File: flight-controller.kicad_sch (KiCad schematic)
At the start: 9 parts, among them J1 USB_C_Receptacle_USB2.0, U1 AT32F435RGT7, U2 BMI270, U3 BMP280, U4 W25N01GVZEIG, U5 AT7456E, U6 TPS54335A, U7 TPS54335A, U8 TLV75733PDBV

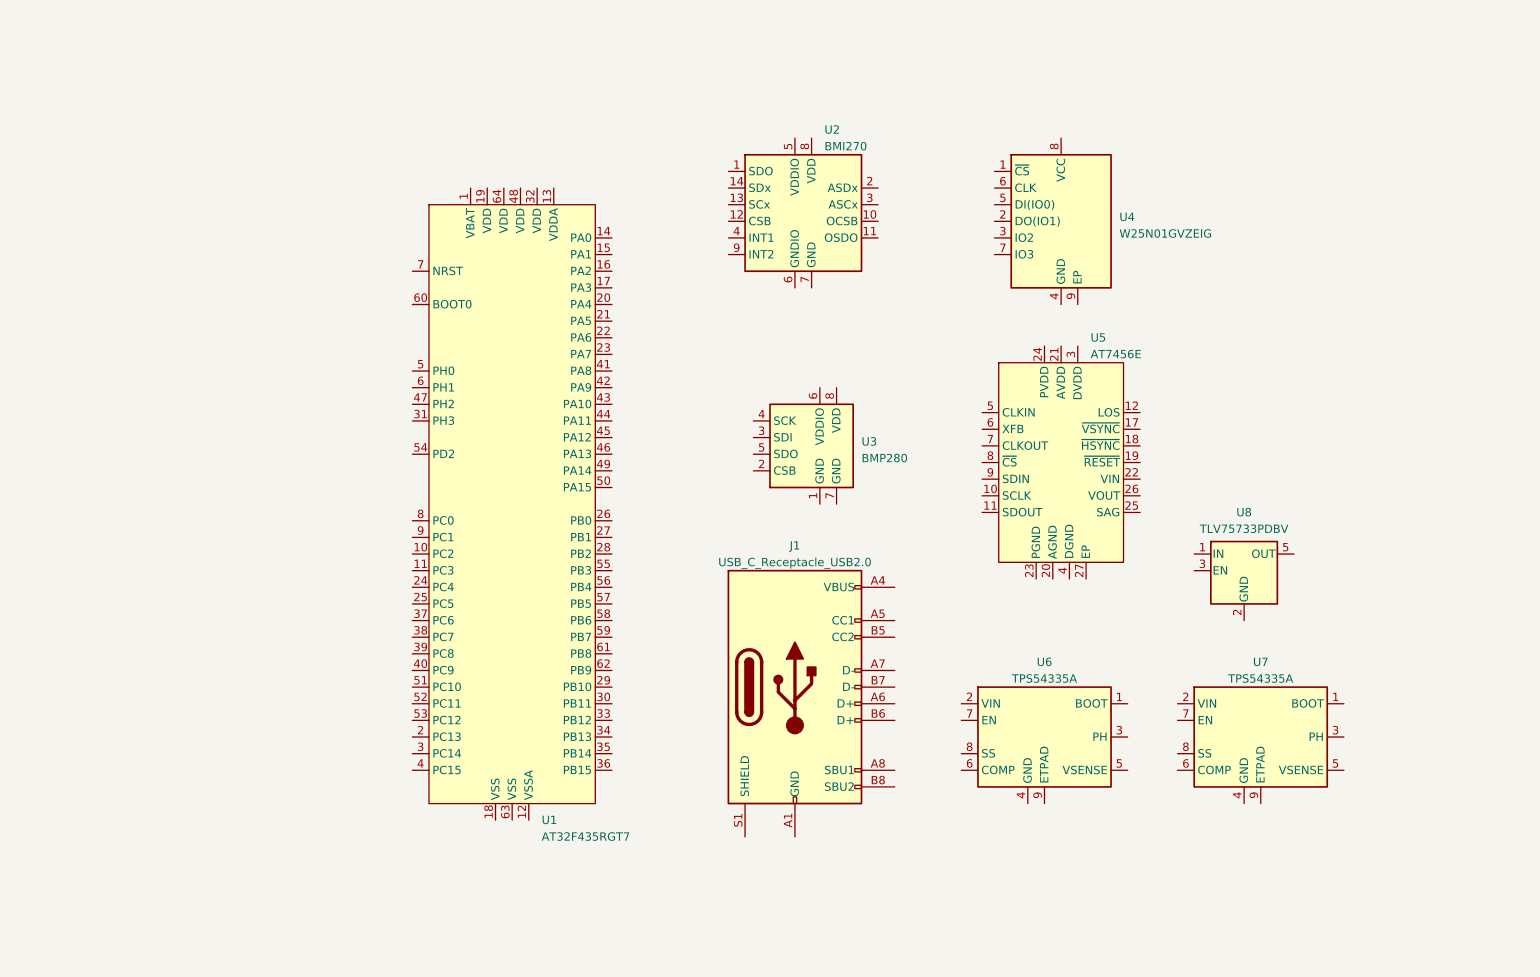
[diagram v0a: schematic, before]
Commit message: Begin AT32 pin planning, add USB footprint, schematic basics
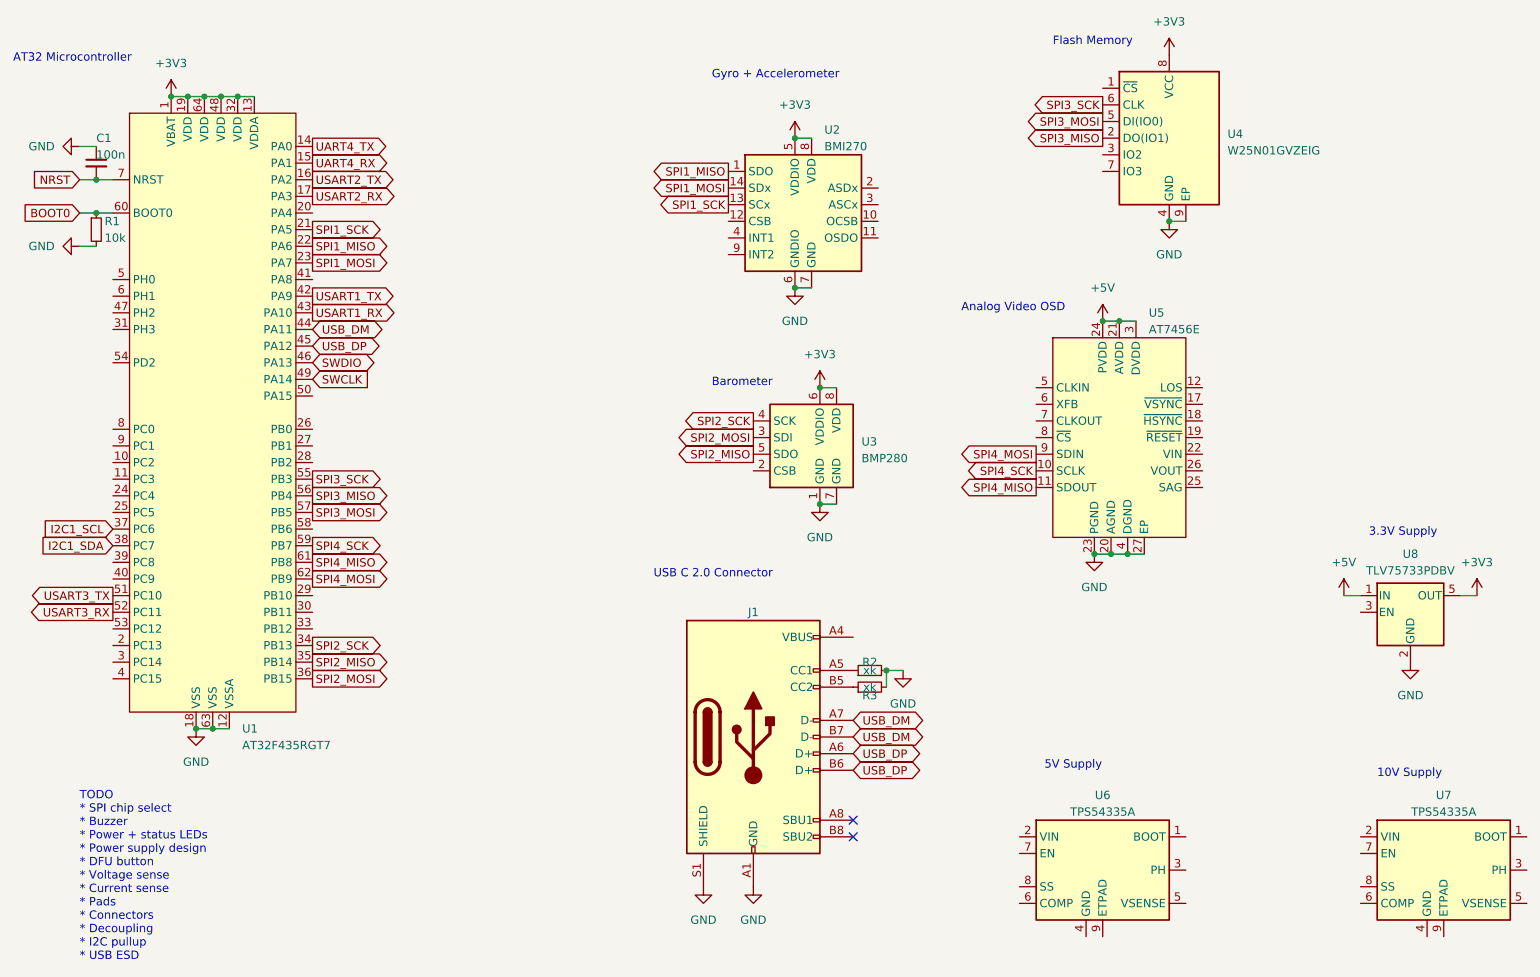
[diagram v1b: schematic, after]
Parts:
- added C1: 100n, symbol Device:C_Small
- added R1: 10k, symbol Device:R_Small
- added R2, R3: xk, symbol Device:R_Small
- J1: footprint (none) -> flight-controller:TYPE-C-31-M-12
- U1: footprint (none) -> Package_QFP:LQFP-64_10x10mm_P0.5mm
- U5: footprint (none) -> Package_SO:TSSOP-28-1EP_4.4x9.7mm_P0.65mm
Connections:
- net +5V: now reaches U8.1 (IN)
- net +5V: now also U5.21 (AVDD), U5.24 (PVDD), U5.3 (DVDD)
- net GND: now reaches U8.2 (GND)
- net GND: now also J1.A1 (GND), J1.A12 (GND), J1.B1 (GND), J1.B12 (GND), J1.S1 (SHIELD), U1.12 (VSSA), U1.18 (VSS), U1.63 (VSS), U2.6 (GNDIO), U2.7 (GND), U3.1 (GND), U3.7 (GND), U4.4 (GND), U4.9 (EP), U5.20 (AGND), U5.23 (PGND), U5.27 (EP), U5.4 (DGND), C1.1, R1.2, R2.2, R3.2
- net +3V3: now reaches U8.5 (OUT)
- net +3V3: now also U1.1 (VBAT), U1.13 (VDDA), U1.19 (VDD), U1.32 (VDD), U1.48 (VDD), U1.64 (VDD), U2.5 (VDDIO), U2.8 (VDD), U3.6 (VDDIO), U3.8 (VDD), U4.8 (VCC)
- net SPI2_MOSI: now reaches U3.3 (SDI)
- net SPI2_MOSI: now also U1.36 (PB15)
- net SPI2_SCK: now reaches U3.4 (SCK)
- net SPI2_SCK: now also U1.34 (PB13)
- net SPI2_MISO: now reaches U3.5 (SDO)
- net SPI2_MISO: now also U1.35 (PB14)
- net SPI1_MISO: now reaches U2.1 (SDO)
- net SPI1_MISO: now also U1.22 (PA6)
- net SPI1_SCK: now reaches U2.13 (SCx)
- net SPI1_SCK: now also U1.21 (PA5)
- net SPI1_MOSI: now reaches U2.14 (SDx)
- net SPI1_MOSI: now also U1.23 (PA7)
- net UART4_TX: now reaches U1.14 (PA0)
- net UART4_RX: now reaches U1.15 (PA1)
- net USART2_TX: now reaches U1.16 (PA2)
- net USART2_RX: now reaches U1.17 (PA3)
- net I2C1_SCL: now reaches U1.37 (PC6)
- net I2C1_SDA: now reaches U1.38 (PC7)
- net USART1_TX: now reaches U1.42 (PA9)
- net USART1_RX: now reaches U1.43 (PA10)
- net USB_DM: now reaches U1.44 (PA11)
- net USB_DM: now also J1.A7 (D-), J1.B7 (D-)
- net USB_DP: now reaches U1.45 (PA12)
- net USB_DP: now also J1.A6 (D+), J1.B6 (D+)
- net SWDIO: now reaches U1.46 (PA13)
- net SWCLK: now reaches U1.49 (PA14)
- net USART3_TX: now reaches U1.51 (PC10)
- net USART3_RX: now reaches U1.52 (PC11)
- net SPI3_SCK: now reaches U1.55 (PB3)
- net SPI3_SCK: now also U4.6 (CLK)
- net SPI3_MISO: now reaches U1.56 (PB4)
- net SPI3_MISO: now also U4.2 (DO(IO1))
- net SPI3_MOSI: now reaches U1.57 (PB5)
- net SPI3_MOSI: now also U4.5 (DI(IO0))
- net SPI4_SCK: now reaches U1.59 (PB7)
- net SPI4_SCK: now also U5.10 (SCLK)
- net BOOT0: now reaches U1.60 (BOOT0)
- net BOOT0: now also R1.1
- net SPI4_MISO: now reaches U1.61 (PB8)
- net SPI4_MISO: now also U5.11 (SDOUT)
- net SPI4_MOSI: now reaches U1.62 (PB9)
- net SPI4_MOSI: now also U5.9 (SDIN)
- net NRST: now reaches U1.7 (NRST)
- net NRST: now also C1.2
- net at J1.A5 (CC1): now also R2.1
- net at J1.B5 (CC2): now also R3.1
- no-connect marks 0 -> 2
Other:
- note added: "10V Supply"
- note added: "3.3V Supply"
- note added: "5V Supply"
- note added: "AT32 Microcontroller"
- note added: "Analog Video OSD"
- note added: "Barometer"
- note added: "Flash Memory"
- note added: "Gyro + Accelerometer"
- note added: "TODO * SPI chip select * Buzzer * Power + status LEDs * Power supply design * DFU button * Voltage sense * Current sense * Pads * Connectors * Decoupling * I2C pullup * USB ESD"
- note added: "USB C 2.0 Connector"
- moved on the sheet: J1, U1, U4, U5, U6, U7, U8

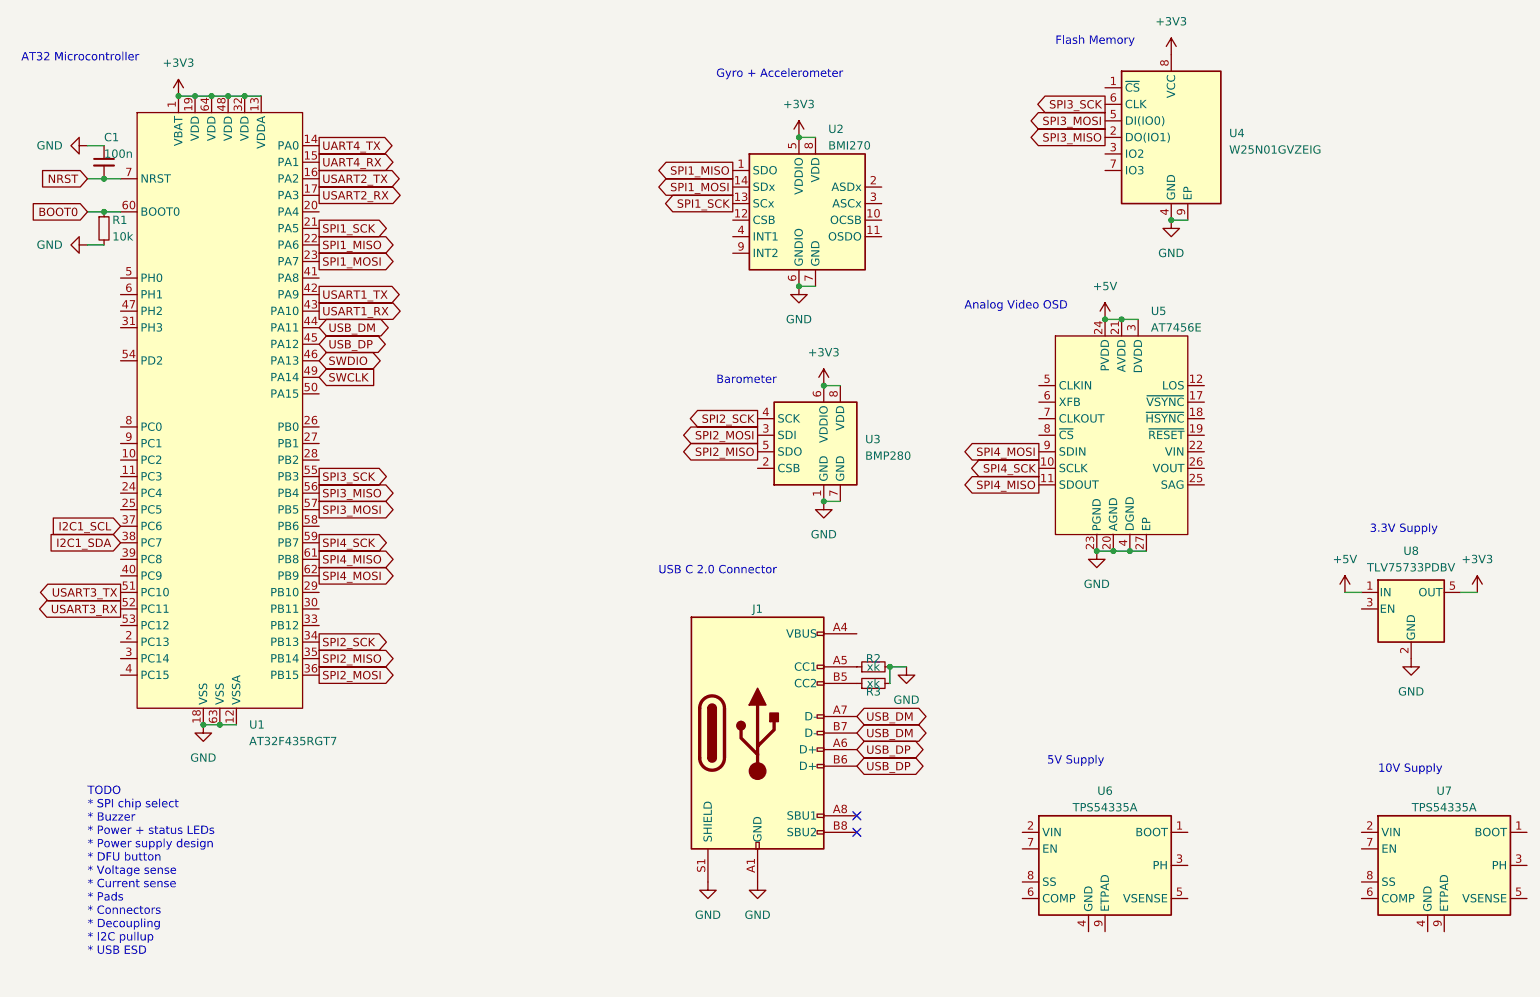
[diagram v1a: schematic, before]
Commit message: Finish majority of MCU pin mapping
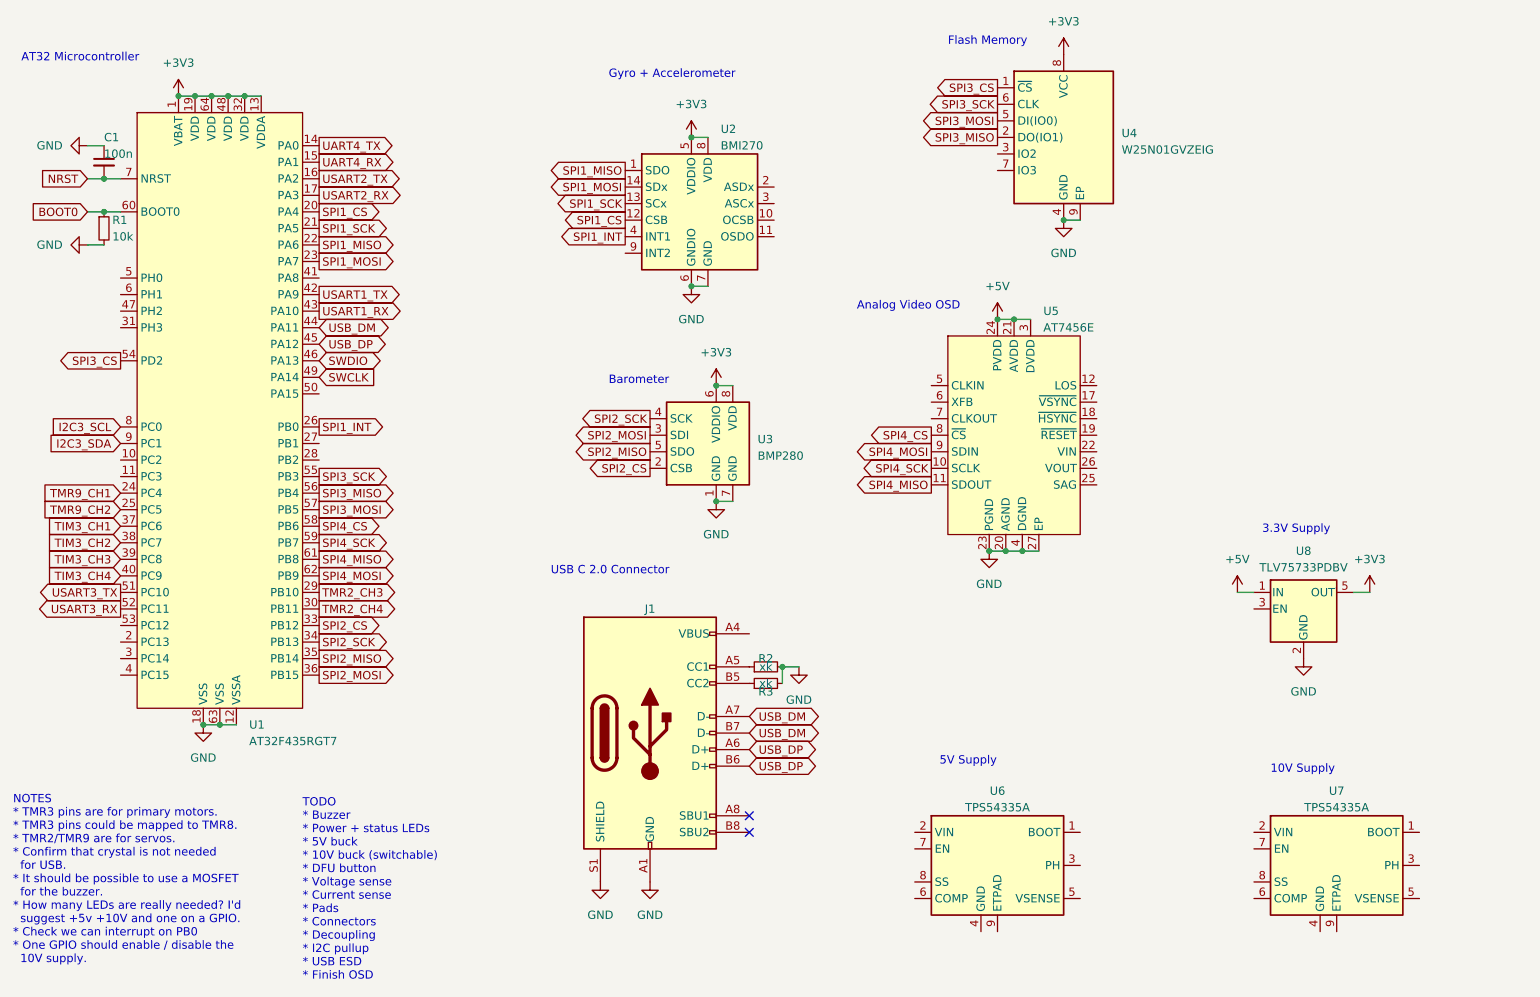
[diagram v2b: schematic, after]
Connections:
- net SPI2_CS: now reaches U3.2 (CSB)
- net SPI2_CS: now also U1.33 (PB12)
- net SPI1_CS: now reaches U2.12 (CSB)
- net SPI1_CS: now also U1.20 (PA4)
- net SPI1_INT: now reaches U2.4 (INT1)
- net SPI1_INT: now also U1.26 (PB0)
- net TMR9_CH1: now reaches U1.24 (PC4)
- net TMR9_CH2: now reaches U1.25 (PC5)
- net TMR2_CH3: now reaches U1.29 (PB10)
- net TMR2_CH4: now reaches U1.30 (PB11)
- net TIM3_CH3: now reaches U1.39 (PC8)
- net TIM3_CH4: now reaches U1.40 (PC9)
- net SPI3_CS: now reaches U1.54 (PD2)
- net SPI3_CS: now also U4.1 (~{CS})
- net SPI4_CS: now reaches U1.58 (PB6)
- net SPI4_CS: now also U5.8 (~{CS})
- net I2C3_SCL: now reaches U1.8 (PC0)
- net I2C3_SDA: now reaches U1.9 (PC1)
- net I2C1_SCL renamed TIM3_CH1
- net I2C1_SDA renamed TIM3_CH2
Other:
- note added: "NOTES * TMR3 pins are for primary motors. * TMR3 pins could be mapped to TMR8. * TMR2/TMR9 are for servos. * Confirm that crystal is not needed for USB. * It should be possible to use a MOSFET for the buzzer. * How many LEDs are really needed? I'd suggest +5v +10V and one on a GPIO. * Check we can interrupt on PB0 * One GPIO should enable / disable the 10V supply."
- note added: "TODO * Buzzer * Power + status LEDs * 5V buck * 10V buck (switchable) * DFU button * Voltage sense * Current sense * Pads * Connectors * Decoupling * I2C pullup * USB ESD * Finish OSD"
- note removed: "TODO * SPI chip select * Buzzer * Power + status LEDs * Power supply design * DFU button * Voltage sense * Current sense * Pads * Connectors * Decoupling * I2C pullup * USB ESD"
- moved on the sheet: J1, R2, R3, U2, U3, U4, U5, U6, U7, U8

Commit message: Tidy up schematic, fix label directions, add decupling caps, pullups, buttons, LEDs
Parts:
- added C10, C11, C12, C13, C14, C15, C2, C3, C4, C5, C6, C7, C8, C9: 100n, symbol Device:C_Small
- added D1: BLUE, symbol Device:LED
- added D2: GREEN, symbol Device:LED
- added D3: RED, symbol Device:LED
- added D4: YELLOW, symbol Device:LED
- added R4, R5: 10k, symbol Device:R_Small
- added R6: 220, symbol Device:R_Small
- added R7, R8, R9: ???, symbol Device:R_Small
- added SW1: SW_Push, symbol Switch:SW_Push
- R2, R3: value xk -> 5.1k
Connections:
- net +3V3: now also U2.2 (ASDx), U2.3 (ASCx), R4.2, R5.2, SW1.2
- net BOOT0: now also SW1.1
- net GND: now also D3.1 (K), D4.1 (K)
- net I2C3_SCL: now also R4.1
- net I2C3_SDA: now also R5.1
- net +BATT: now reaches U7.2 (VIN)
- net +BATT: now also U6.2 (VIN)
- new net: D2.2 (A), R7.2
- new net: D3.2 (A), R8.2
- new net: R6.1, R7.1, R8.1
- new net: D1.2 (A), R6.2
- new net: D4.2 (A), R9.2
- new net +10V: R9.1
- new net LED1: D1.1 (K)
- new net LED2: D2.1 (K)
- no-connect marks 2 -> 7
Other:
- note added: "3v3 or 5V"
- note added: "Buttons and LEDs"
- note added: "Buzzer"
- note added: "Connectors"
- note added: "I2C Pullup"
- note added: "NOTES * TMR3 pins are for primary motors. * TMR3 pins could be mapped to TMR8. * TMR2/TMR9 are for servos. * Confirm that crystal is not needed for USB. * It should be possible to use a MOSFET for the buzzer. * How many LEDs are really needed? I'd suggest +5v +10V and one on a GPIO. * Check we can interrupt on PB0 * One GPIO should enable / disable the 10V supply. * LED supplies can be 5V as long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"
- note added: "TODO * Buzzer * 5V buck * 10V buck (switchable) * Voltage sense * Current sense * Pads * Connectors * USB ESD * Finish OSD"
- note added: "USB ESD"
- note removed: "NOTES * TMR3 pins are for primary motors. * TMR3 pins could be mapped to TMR8. * TMR2/TMR9 are for servos. * Confirm that crystal is not needed for USB. * It should be possible to use a MOSFET for the buzzer. * How many LEDs are really needed? I'd suggest +5v +10V and one on a GPIO. * Check we can interrupt on PB0 * One GPIO should enable / disable the 10V supply."
- note removed: "TODO * Buzzer * Power + status LEDs * 5V buck * 10V buck (switchable) * DFU button * Voltage sense * Current sense * Pads * Connectors * Decoupling * I2C pullup * USB ESD * Finish OSD"
- moved on the sheet: C1, J1, R1, R2, R3, U1, U2, U3, U4, U5, U6, U7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

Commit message: Add buzzer and power supply designs for consideration
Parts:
- removed U6, U7: TPS54335A, Package_SO:TI_SO-PowerPAD-8_ThermalVias, symbol Regulator_Switching:TPS54336ADDA
- added C16: 47p, symbol Device:C_Small
- added C17: 47u, symbol Device:C
- added C18, C20: 100n, symbol Device:C_Small
- added C19, C21, C25, C26: 10u, symbol Device:C
- added C22: 82p, symbol Device:C_Small
- added C23, C24: 22u, symbol Device:C
- added L1, L2: 10u, symbol Device:L
- added Q1: NMOS, symbol Simulation_SPICE:NMOS
- added R10, R12: 100k, symbol Device:R_Small
- added R11: 6.34k, symbol Device:R_Small
- added R13: 13.7k, symbol Device:R_Small
- added R14: 10k, symbol Device:R_Small
- added U6, U7: TPS54302, Package_TO_SOT_SMD:SOT-23-6, symbol Regulator_Switching:TPS54302
- added U9: USBLC6-2P6, Package_TO_SOT_SMD:SOT-666, symbol Power_Protection:USBLC6-2P6
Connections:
- net +10V: now also C22.1, C23.1, C24.1, L2.2, R10.1
- net +3V3: now also C10.1, C11.1, C12.1, C13.1, C14.1, C15.1, C2.1, C3.1, C25.1
- net +5V: now also R6.1, R7.1, R8.1, U8.3 (EN), C16.1, C17.1, C26.1, L1.2, R12.1
- net +BATT: now also C19.1, C21.1, U6.3 (VIN), U7.3 (VIN)
- net 10V_SW: now also U7.5 (EN)
- net BUZZ: now also Q1.2 (G), R14.1
- net GND: now also C10.2, C11.2, C12.2, C13.2, C14.2, C15.2, C2.2, C3.2, C17.2, C19.2, C21.2, C23.2, C24.2, C25.2, C26.2, Q1.3 (S), R11.2, R13.2, R14.2, U6.1 (GND), U7.1 (GND), U9.2 (GND)
- net USB_DM: now also U9.3 (I/O2); no longer J1.A7 (D-), J1.B7 (D-)
- net USB_DP: now also U9.1 (I/O1); no longer J1.A6 (D+), J1.B6 (D+)
- net VBUS: now reaches J1.A4 (VBUS), J1.A9 (VBUS), J1.B4 (VBUS), J1.B9 (VBUS)
- net VBUS: now also U9.5 (VBUS)
- new net: C20.2, L1.1, U6.2 (SW)
- new net: C18.2, L2.1, U7.2 (SW)
- new net: C22.2, R10.2, R11.1, U7.4 (FB)
- new net: C16.2, R12.2, R13.1, U6.4 (FB)
- new net: C18.1, U7.6 (BOOT)
- new net: C20.1, U6.6 (BOOT)
- new net BUZZER-: Q1.1 (D)
- new net EUSB_DM: J1.A7 (D-), J1.B7 (D-), U9.4 (I/O2)
- new net EUSB_DP: J1.A6 (D+), J1.B6 (D+), U9.6 (I/O1)
- no-connect marks 7 -> 8
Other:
- note added: "NOTES * TMR3 pins are for primary motors. * TMR3 pins could be mapped to TMR8. * TMR2/TMR9 are for servos. * Confirm that crystal is not needed for USB. * Check we can interrupt on PB0 * LED supplies can be 5V as long as LED pins on MCU are FT. * Consider TagConnect for SWD"
- note added: "THIS BLOCK IS INCOMPLETE"
- note added: "TODO * Voltage sense * Current sense * Pads * Connectors * OSD"
- note removed: "3v3 or 5V"
- note removed: "Connectors"
- note removed: "NOTES * TMR3 pins are for primary motors. * TMR3 pins could be mapped to TMR8. * TMR2/TMR9 are for servos. * Confirm that crystal is not needed for USB. * It should be possible to use a MOSFET for the buzzer. * How many LEDs are really needed? I'd suggest +5v +10V and one on a GPIO. * Check we can interrupt on PB0 * One GPIO should enable / disable the 10V supply. * LED supplies can be 5V as long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"
- note removed: "TODO * Buzzer * 5V buck * 10V buck (switchable) * Voltage sense * Current sense * Pads * Connectors * USB ESD * Finish OSD"
- moved on the sheet: C2, C3, D1, D2, D3, D4, R4, R5, R6, R7, R8, R9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
